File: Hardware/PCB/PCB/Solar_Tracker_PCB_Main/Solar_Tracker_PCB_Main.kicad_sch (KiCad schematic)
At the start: 0 parts

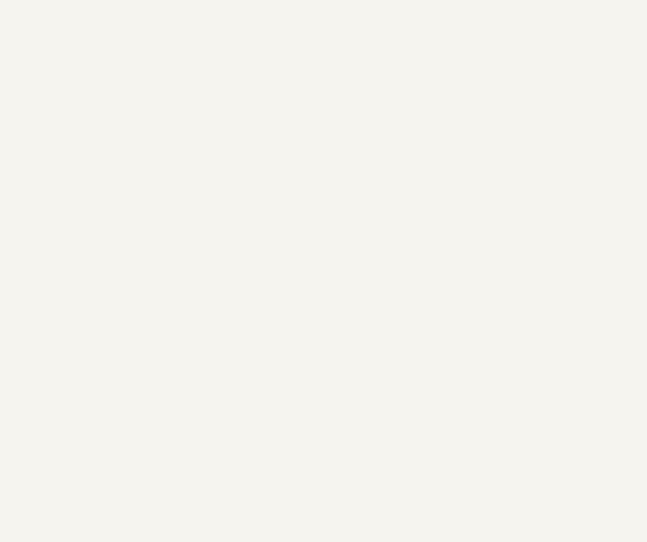
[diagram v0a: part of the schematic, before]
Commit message: Agregue el sensor
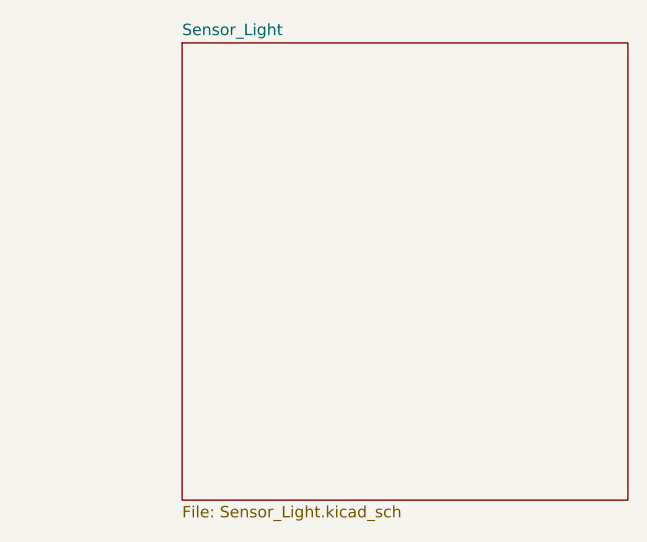
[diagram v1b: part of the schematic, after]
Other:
- added sheet Sensor_Light (Sensor_Light.kicad_sch)
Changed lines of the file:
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@@
+		)
+	)
+	(sheet
+		(at 152.4 27.94)
+		(size 49.53 50.8)
+		(exclude_from_sim no)
+		(in_bom yes)
+		(on_board yes)
+		(dnp no)
+		(fields_autoplaced yes)
+		(stroke
+			(width 0.1524)
+			(type solid)
+		)
+		(fill
+			(color 0 0 0 0.0000)
+		)
+		(property "Sheetname" "Sensor_Light"
+			(at 152.4 27.2284 0)
+			(effects
+				(font
+					(size 1.27 1.27)
+				)
+				(justify left bottom)
+			)
+		)
+		(property "Sheetfile" "Sensor_Light.kicad_sch"
+			(at 152.4 79.3246 0)
+			(effects
+				(font
+					(size 1.27 1.27)
+				)
+				(justify left top)
+			)
+		)
+		(instances
+			(project "Solar_Tracker_PCB_Main"
+				(path "/99b6ddd9-7ffe-4c85-972a-e0f594a166d4"
+					(page "3")
+				)
+			)
 		)
 	)

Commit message: Actualizacion PCB
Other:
- added sheet IMU (IMU.kicad_sch)
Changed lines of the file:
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@@
+	)
+	(sheet
+		(at 35.56 101.6)
+		(size 44.45 31.75)
+		(exclude_from_sim no)
+		(in_bom yes)
+		(on_board yes)
+		(dnp no)
+		(fields_autoplaced yes)
+		(stroke
+			(width 0.1524)
+			(type solid)
+		)
+		(fill
+			(color 0 0 0 0.0000)
+		)
+		(property "Sheetname" "IMU"
+			(at 35.56 100.8884 0)
+			(effects
+				(font
+					(size 1.27 1.27)
+				)
+				(justify left bottom)
+			)
+		)
+		(property "Sheetfile" "IMU.kicad_sch"
+			(at 35.56 133.9346 0)
+			(effects
+				(font
+					(size 1.27 1.27)
+				)
+				(justify left top)
+			)
+		)
+		(instances
+			(project "Solar_Tracker_PCB_Main"
+				(path "/99b6ddd9-7ffe-4c85-972a-e0f594a166d4"
+					(page "4")
+				)
+			)
+		)
 	)
 	(sheet

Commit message: actualizacion de pcb (IMU)
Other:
- removed sheet Sensor_Light
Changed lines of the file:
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@@
-		)
-	)
-	(sheet
-		(at 152.4 27.94)
-		(size 49.53 50.8)
-		(exclude_from_sim no)
-		(in_bom yes)
-		(on_board yes)
-		(dnp no)
-		(fields_autoplaced yes)
-		(stroke
-			(width 0.1524)
-			(type solid)
-		)
-		(fill
-			(color 0 0 0 0.0000)
-		)
-		(property "Sheetname" "Sensor_Light"
-			(at 152.4 27.2284 0)
-			(effects
-				(font
-					(size 1.27 1.27)
-				)
-				(justify left bottom)
-			)
-		)
-		(property "Sheetfile" "Sensor_Light.kicad_sch"
-			(at 152.4 79.3246 0)
-			(effects
-				(font
-					(size 1.27 1.27)
-				)
-				(justify left top)
-			)
-		)
-		(instances
-			(project "Solar_Tracker_PCB_Main"
-				(path "/99b6ddd9-7ffe-4c85-972a-e0f594a166d4"
-					(page "3")
-				)
-			)
 		)
 	)

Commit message: actualizacion pcb main
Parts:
- added J1: MTJ-88ARX1-FSM-LG, MTJ-88ARX1:MTJ88ARX1FSMLG, symbol MTJ-88ARX1-FSM-LG:MTJ-88ARX1-FSM-LG
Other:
- note added: "RJ45 FEMALE"
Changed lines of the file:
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@@
 	(generator_version "9.0")
 	(paper "A4")
+	(rectangle
+		(start 236.22 12.7)
+		(end 284.48 59.69)
+		(stroke
+			(width 0)
+			(type default)
+		)
+		(fill
+			(type none)
+		)
+	)
+	(text "RJ45 FEMALE"
+		(exclude_from_sim no)
+		(at 260.35 20.32 0)
+		(effects
+			(font
+				(size 1.27 1.27)
+			)
+		)
+	)
+	(symbol
+		(lib_id "MTJ-88ARX1-FSM-LG:MTJ-88ARX1-FSM-LG")
+		(at 250.19 34.29 0)
+		(unit 1)
+		(exclude_from_sim no)
+		(in_bom yes)
+		(on_board yes)
+		(dnp no)
+		(fields_autoplaced yes)
+		(property "Reference" "J1"
+			(at 261.62 26.67 0)
+			(effects
+				(font
+					(size 1.27 1.27)
+				)
+			)
+		)
+		(property "Value" "MTJ-88ARX1-FSM-LG"
+			(at 261.62 29.21 0)
+			(effects
+				(font
+					(size 1.27 1.27)
+				)
+			)
+		)
+		(property "Footprint" "MTJ-88ARX1:MTJ88ARX1FSMLG"
+			(at 269.24 129.21 0)
+			(effects
+				(font
+					(size 1.27 1.27)
+				)
+				(justify left top)
+				(hide yes)
+			)
+		)
+		(property "Datasheet" "https://www.arrow.com/en/products/mtj-88arx1-fsm-lg/adam-tech"
+			(at 269.24 229.21 0)
+			(effects
+				(font
+					(size 1.27 1.27)
+				)
+				(justify left top)
+				(hide yes)
+			)
+		)
+		(property "Description" "RJ45 Modular Jack, Shielded, Dip, Side Entry,LEDs"
+			(at 250.19 34.29 0)
+			(effects
+				(font
+					(size 1.27 1.27)
+				)
+				(hide yes)
+			)
+		)
+		(property "Height" "13.708"
+			(at 269.24 429.21 0)
+			(effects
+				(font
+					(size 1.27 1.27)
+				)
+				(justify left top)
+				(hide yes)
+			)
+		)
+		(property "Mouser Part Number" "737-MTJ88ARX1FSMLG"
+			(at 269.24 529.21 0)
+			(effects
+				(font
+					(size 1.27 1.27)
+				)
+				(justify left top)
+				(hide yes)
+			)
+		)
+		(property "Mouser Price/Stock" "https://www.mouser.co.uk/ProductDetail/Adam-Tech/MTJ-88ARX1-FSM-LG?qs=HoCaDK9Nz5cwcndn7zcdzQ%3D%3D"
+			(at 269.24 629.21 0)
+			(effects
+				(font
+					(size 1.27 1.27)
+				)
+				(justify left top)
+				(hide yes)
+			)
+		)
+		(property "Manufacturer_Name" "Adam Tech"
+			(at 269.24 729.21 0)
+			(effects
+				(font
+					(size 1.27 1.27)
+				)
+				(justify left top)
+				(hide yes)
+			)
+		)
+		(property "Manufacturer_Part_Number" "MTJ-88ARX1-FSM-LG"
+			(at 269.24 829.21 0)
+			(effects
+				(font
+					(size 1.27 1.27)
+				)
+				(justify left top)
+				(hide yes)
+			)
+		)
+		(pin "11"
+		)
+		(pin "MH1"
+		)
+		(pin "MH2"
+		)
+		(pin "1"
+		)
+		(pin "4"
+		)
+		(pin "5"
+		)
+		(pin "8"
+		)
+		(pin "10"
+		)
+		(pin "6"
+		)
+		(pin "3"
+		)
+		(pin "7"
+		)
+		(pin "2"
+		)
+		(pin "9"
+		)
+		(pin "12"
+		)
+		(instances
+			(project ""
+				(path "/99b6ddd9-7ffe-4c85-972a-e0f594a166d4"
+					(reference "J1")
+					(unit 1)
+				)
+			)
+		)
+	)
 	(sheet
 		(at 41.91 29.21)

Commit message: actualizacion pcb main
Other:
- added sheet BUCK CONVERTER (buck.kicad_sch)
- moved on the sheet: J1
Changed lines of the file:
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@@
 	(symbol
 		(lib_id "MTJ-88ARX1-FSM-LG:MTJ-88ARX1-FSM-LG")
-		(at 250.19 34.29 0)
+		(at 248.92 33.02 0)
 		(unit 1)
 		(exclude_from_sim no)
@@
 		(fields_autoplaced yes)
 		(property "Reference" "J1"
-			(at 261.62 26.67 0)
+			(at 260.35 25.4 0)
 			(effects
 				(font
@@
 		)
 		(property "Value" "MTJ-88ARX1-FSM-LG"
-			(at 261.62 29.21 0)
+			(at 260.35 27.94 0)
 			(effects
 				(font
@@
 		)
 		(property "Footprint" "MTJ-88ARX1:MTJ88ARX1FSMLG"
-			(at 269.24 129.21 0)
+			(at 267.97 127.94 0)
 			(effects
 				(font
@@
 		)
 		(property "Datasheet" "https://www.arrow.com/en/products/mtj-88arx1-fsm-lg/adam-tech"
-			(at 269.24 229.21 0)
+			(at 267.97 227.94 0)
 			(effects
 				(font
@@
 		)
 		(property "Description" "RJ45 Modular Jack, Shielded, Dip, Side Entry,LEDs"
-			(at 250.19 34.29 0)
+			(at 248.92 33.02 0)
 			(effects
 				(font
@@
 		)
 		(property "Height" "13.708"
-			(at 269.24 429.21 0)
+			(at 267.97 427.94 0)
 			(effects
 				(font
@@
 		)
 		(property "Mouser Part Number" "737-MTJ88ARX1FSMLG"
-			(at 269.24 529.21 0)
+			(at 267.97 527.94 0)
 			(effects
 				(font
@@
 		)
 		(property "Mouser Price/Stock" "https://www.mouser.co.uk/ProductDetail/Adam-Tech/MTJ-88ARX1-FSM-LG?qs=HoCaDK9Nz5cwcndn7zcdzQ%3D%3D"
-			(at 269.24 629.21 0)
+			(at 267.97 627.94 0)
 			(effects
 				(font
@@
 		)
 		(property "Manufacturer_Name" "Adam Tech"
-			(at 269.24 729.21 0)
+			(at 267.97 727.94 0)
 			(effects
 				(font
@@
 		)
 		(property "Manufacturer_Part_Number" "MTJ-88ARX1-FSM-LG"
-			(at 269.24 829.21 0)
+			(at 267.97 827.94 0)
 			(effects
 				(font
@@
 				)
 			)
+		)
+	)
+	(sheet
+		(at 115.57 34.29)
+		(size 53.34 41.91)
+		(exclude_from_sim no)
+		(in_bom yes)
+		(on_board yes)
+		(dnp no)
+		(fields_autoplaced yes)
+		(stroke
+			(width 0.1524)
+			(type solid)
+		)
+		(fill
+			(color 0 0 0 0.0000)
+		)
+		(property "Sheetname" "BUCK CONVERTER"
+			(at 115.57 33.5784 0)
+			(effects
+				(font
+					(size 1.27 1.27)
+				)
+				(justify left bottom)
+			)
+		)
+		(property "Sheetfile" "buck.kicad_sch"
+			(at 115.57 76.7846 0)
+			(effects
+				(font
+					(size 1.27 1.27)
+				)
+				(justify left top)
+			)
+		)
+		(instances
+			(project "Solar_Tracker_PCB_Main"
+				(path "/99b6ddd9-7ffe-4c85-972a-e0f594a166d4"
+					(page "4")
+				)
+			)

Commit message: Actualizacion PCB Principal
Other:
- added sheet RTC (RTC.kicad_sch)
- sheet BUCK CONVERTER: file buck.kicad_sch -> BUCK.kicad_sch
- sheet MCU: file untitled.kicad_sch -> MCU.kicad_sch
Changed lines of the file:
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@@
 	)
 	(sheet
-		(at 41.91 29.21)
-		(size 44.45 43.18)
+		(at 17.78 21.59)
+		(size 44.45 41.91)
 		(exclude_from_sim no)
 		(in_bom yes)
@@
 		)
 		(property "Sheetname" "MCU"
-			(at 41.91 28.4984 0)
+			(at 17.78 20.8784 0)
 			(effects
 				(font
@@
 			)
 		)
-		(property "Sheetfile" "untitled.kicad_sch"
-			(at 41.91 72.9746 0)
+		(property "Sheetfile" "MCU.kicad_sch"
+			(at 17.78 64.0846 0)
 			(effects
 				(font
@@
 	)
 	(sheet
-		(at 115.57 34.29)
-		(size 53.34 41.91)
+		(at 64.77 21.59)
+		(size 45.72 41.91)
 		(exclude_from_sim no)
 		(in_bom yes)
@@
 		)
 		(property "Sheetname" "BUCK CONVERTER"
-			(at 115.57 33.5784 0)
+			(at 64.77 20.8784 0)
 			(effects
 				(font
@@
 			)
 		)
-		(property "Sheetfile" "buck.kicad_sch"
-			(at 115.57 76.7846 0)
+		(property "Sheetfile" "BUCK.kicad_sch"
+			(at 64.77 64.0846 0)
 			(effects
 				(font
@@
 	)
 	(sheet
-		(at 35.56 101.6)
-		(size 44.45 31.75)
+		(at 16.51 78.74)
+		(size 44.45 48.26)
+		(exclude_from_sim no)
+		(in_bom yes)
+		(on_board yes)
+		(dnp no)
+		(fields_autoplaced yes)
+		(stroke
+			(width 0.1524)
+			(type solid)
+		)
+		(fill
+			(color 0 0 0 0.0000)
+		)
+		(property "Sheetname" "RTC"
+			(at 16.51 78.0284 0)
+			(effects
+				(font
+					(size 1.27 1.27)
+				)
+				(justify left bottom)
+			)
+		)
+		(property "Sheetfile" "RTC.kicad_sch"
+			(at 16.51 127.5846 0)
+			(effects
+				(font
+					(size 1.27 1.27)
+				)
+				(justify left top)
+			)
+		)
+		(instances
+			(project "Solar_Tracker_PCB_Main"
+				(path "/99b6ddd9-7ffe-4c85-972a-e0f594a166d4"
+					(page "5")
+				)
+			)
+		)
+	)
+	(sheet
+		(at 113.03 21.59)
+		(size 44.45 41.91)
 		(exclude_from_sim no)
 		(in_bom yes)
@@
 		)
 		(property "Sheetname" "IMU"
-			(at 35.56 100.8884 0)
+			(at 113.03 20.8784 0)
 			(effects
 				(font
@@
 		)
 		(property "Sheetfile" "IMU.kicad_sch"
-			(at 35.56 133.9346 0)
+			(at 113.03 64.0846 0)
 			(effects
 				(font

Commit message: Actualizacion PCB Principal
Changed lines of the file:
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@@
 	)
 	(sheet
-		(at 16.51 78.74)
-		(size 44.45 48.26)
+		(at 158.75 21.59)
+		(size 44.45 41.91)
 		(exclude_from_sim no)
 		(in_bom yes)
@@
 		)
 		(property "Sheetname" "RTC"
-			(at 16.51 78.0284 0)
+			(at 158.75 20.8784 0)
 			(effects
 				(font
@@
 		)
 		(property "Sheetfile" "RTC.kicad_sch"
-			(at 16.51 127.5846 0)
+			(at 158.75 64.0846 0)
 			(effects
 				(font

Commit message: actualizacion de pcb
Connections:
- no-connect marks 0 -> 14
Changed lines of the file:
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@@
 		)
+	)
+	(no_connect
+		(at 248.92 38.1)
+	)
+	(no_connect
+		(at 271.78 33.02)
+	)
+	(no_connect
+		(at 248.92 35.56)
+	)
+	(no_connect
+		(at 248.92 48.26)
+	)
+	(no_connect
+		(at 271.78 38.1)
+	)
+	(no_connect
+		(at 248.92 43.18)
+	)
+	(no_connect
+		(at 271.78 40.64)
+	)
+	(no_connect
+		(at 271.78 35.56)
+	)
+	(no_connect
+		(at 248.92 33.02)
+	)
+	(no_connect
+		(at 271.78 48.26)
+	)
+	(no_connect
+		(at 271.78 45.72)
+	)
+	(no_connect
+		(at 248.92 40.64)
+	)
+	(no_connect
+		(at 248.92 45.72)
+	)
+	(no_connect
+		(at 271.78 43.18)
 	)
 	(symbol
